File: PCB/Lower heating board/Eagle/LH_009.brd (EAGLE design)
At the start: 142.8 x 97.5 mm, 8 parts, among them X1 MKDSN1,5/4-5,08

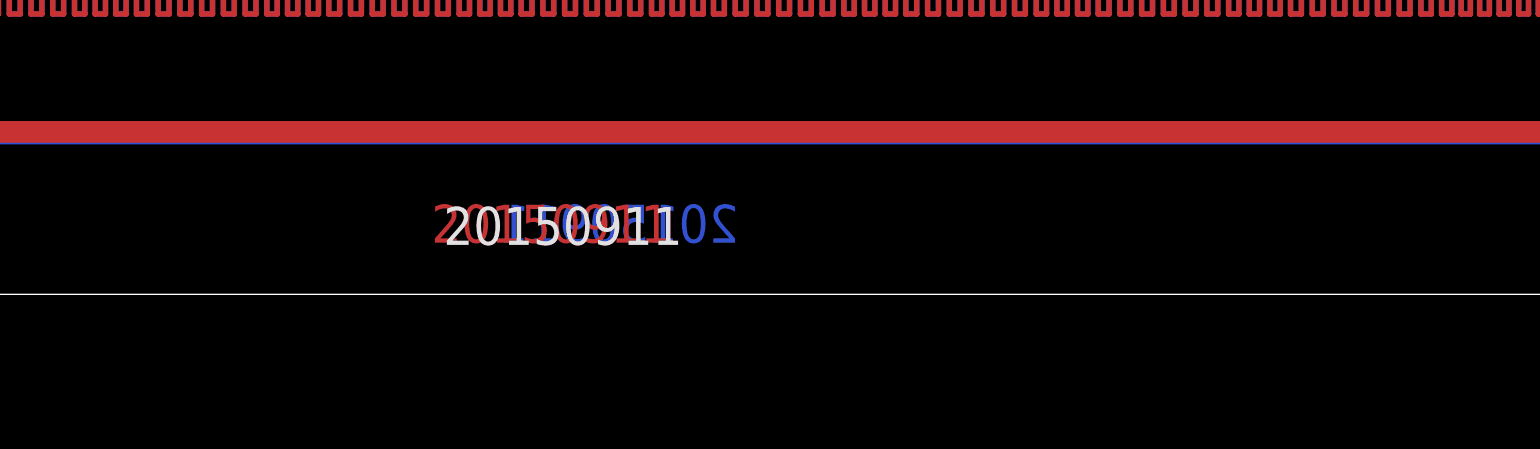
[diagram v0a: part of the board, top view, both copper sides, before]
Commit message: PCB modification, CERN license
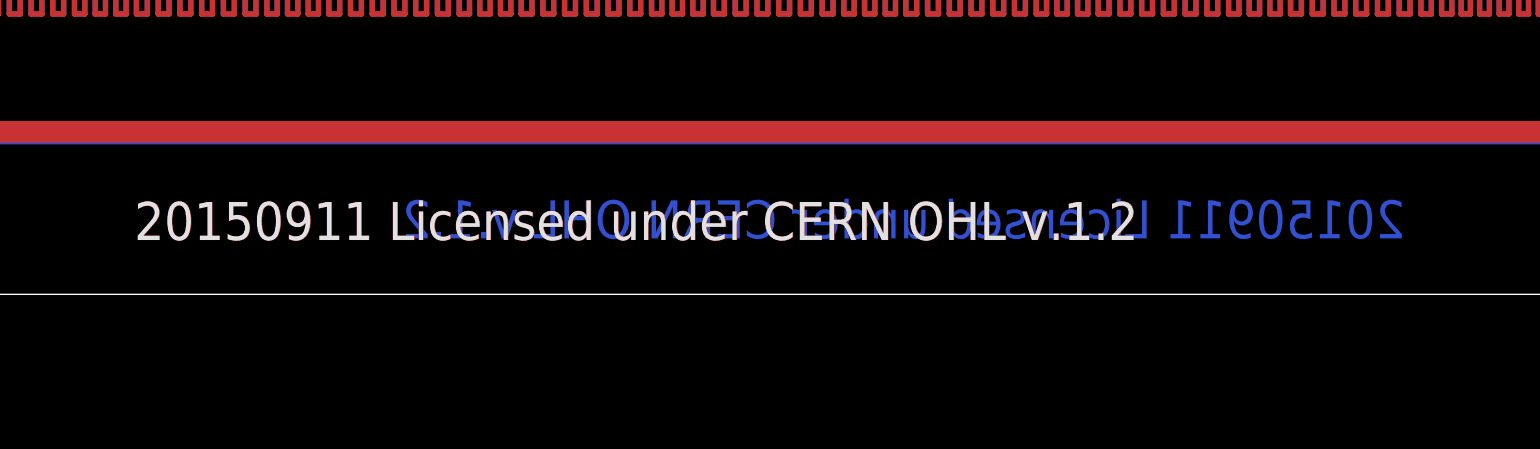
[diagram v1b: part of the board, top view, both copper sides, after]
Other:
- board text added: "20150911 Licensed under CERN OHL v.1.2"
- board text removed: "20150911"
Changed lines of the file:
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@@
 <text x="64.5046" y="93.5768" size="1.778" layer="1" font="vector" ratio="15">Miriam</text>
 <text x="64.1204" y="95.2532" size="1.778" layer="16" font="vector" ratio="15" rot="MR180">Miriam</text>
-<text x="71.755" y="2.413" size="1.778" layer="16" font="vector" ratio="15" rot="MR0">20150911</text>
-<text x="57.404" y="2.413" size="1.778" layer="1" font="vector" ratio="15">20150911</text>
+<text x="102.9208" y="2.6162" size="1.778" layer="16" font="vector" ratio="15" rot="MR0">20150911 Licensed under CERN OHL v.1.2</text>
+<text x="43.5356" y="2.54" size="1.778" layer="1" font="vector" ratio="15">20150911 Licensed under CERN OHL v.1.2</text>
 <rectangle x1="56.642" y1="91.948" x2="81.407" y2="96.5962" layer="41"/>
 <rectangle x1="56.642" y1="91.948" x2="81.407" y2="96.5962" layer="42"/>
-<rectangle x1="56.896" y1="1.778" x2="72.39" y2="4.699" layer="41"/>
-<rectangle x1="56.896" y1="1.778" x2="72.39" y2="4.699" layer="42"/>
 <text x="131.957" y="45.504" size="1.27" layer="21" font="vector" rot="R90">Therm</text>
 <text x="131.937" y="51.954" size="1.27" layer="21" rot="R90">GND</text>
@@
 <text x="64.0188" y="95.431" size="1.778" layer="26" font="vector" ratio="15" rot="MR180">Miriam</text>
 <text x="64.5046" y="93.653" size="1.778" layer="25" font="vector" ratio="15">Miriam</text>
-<text x="57.9628" y="2.3114" size="1.778" layer="25" font="vector" ratio="15">20150911</text>
-<text x="70.7644" y="2.4892" size="1.778" layer="26" font="vector" ratio="15" rot="MR0">20150911</text>
+<text x="43.5102" y="2.54" size="1.778" layer="25" font="vector" ratio="15">20150911 Licensed under CERN OHL v.1.2</text>
+<text x="102.9716" y="2.6162" size="1.778" layer="26" font="vector" ratio="15" rot="MR0">20150911 Licensed under CERN OHL v.1.2</text>
+<rectangle x1="42.3926" y1="1.4478" x2="103.9876" y2="5.1562" layer="41"/>
+<rectangle x1="42.3164" y1="1.4478" x2="103.9876" y2="5.207" layer="42"/>
 </plain>
 <attributes>
